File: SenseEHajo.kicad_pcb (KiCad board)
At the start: 2 copper layers, 141 x 56.9 mm, 104 parts, among them IC1 AP3012, IC2 MCP3221, IC3 74LVC1G125, IC4 K814P, IC5 74LVC1G125, IC6 74LVC1G125, IC7 74LVC1G10, J1 Conn_01x02_Male, J2 REED, J3 RTC ( DS3231), J4 Heizung L, J5 Pumpe L, J6 Conn_01x05, J7 L, J8 N, J9 Prog, Q1 BSS138, SW2 SW1 ( Boot ), SW3 MACHINE_SW2, SW4 MACHINE_SW3, T1 QJ8025, T2 QJ8025, U1 ESP32-WROOM-32, U2 MCP6001-OT, U3 MOC3043M, U4 MOC3043M, U5 MCP6001-OT, U6 LM1117-3.3

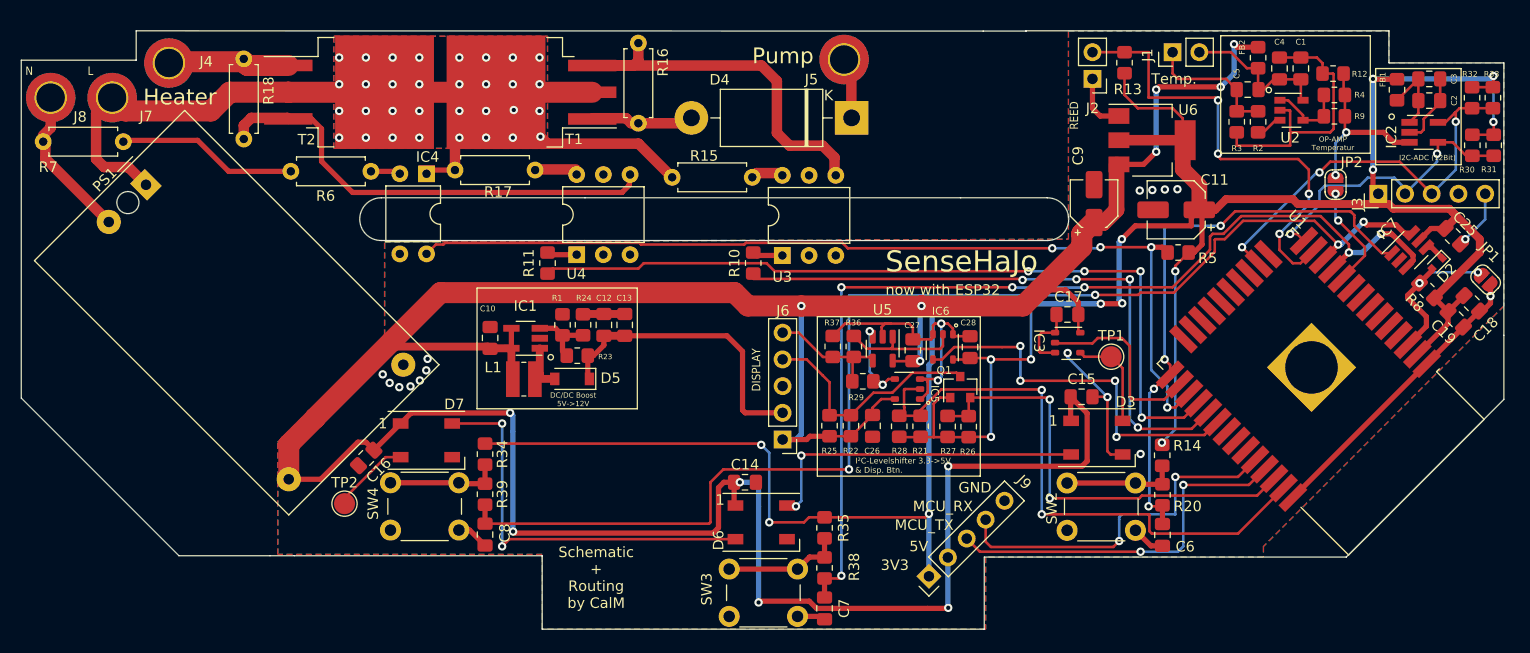
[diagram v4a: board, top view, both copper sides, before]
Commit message: Fix Display BTP senese for press
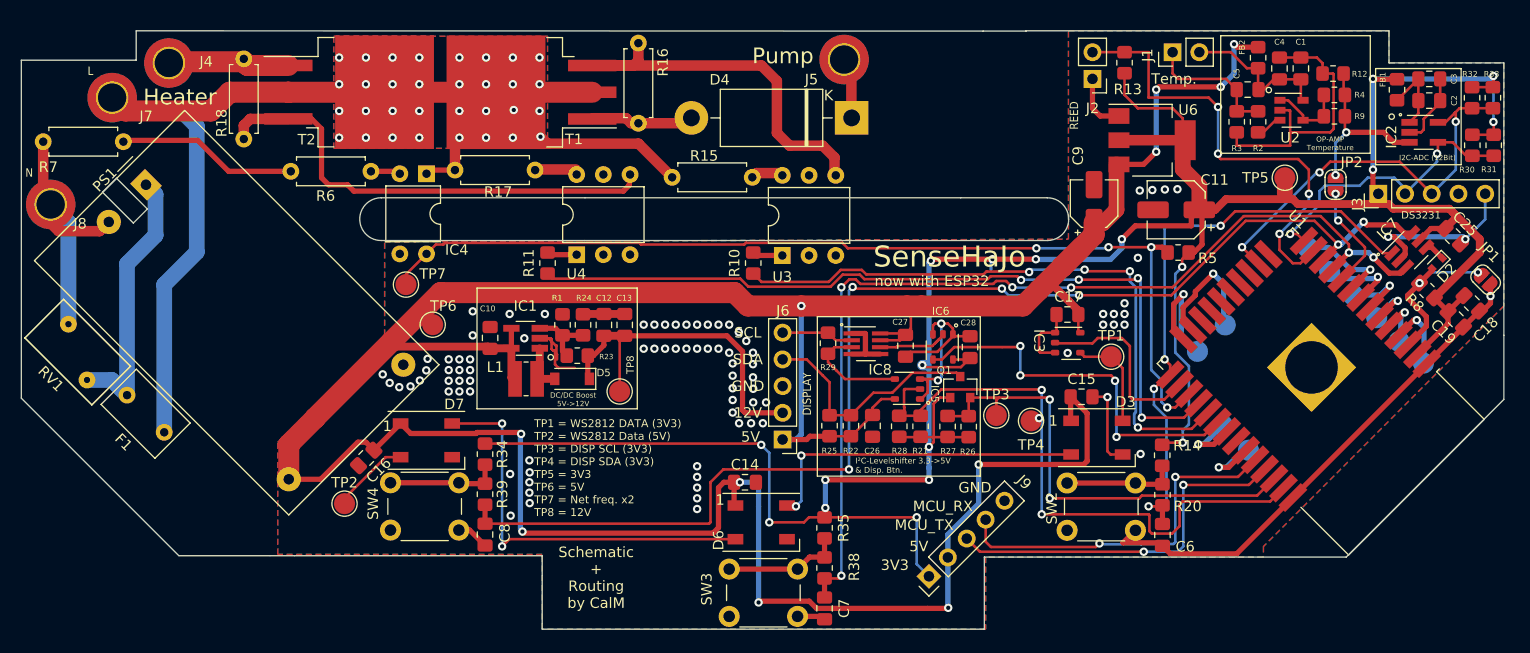
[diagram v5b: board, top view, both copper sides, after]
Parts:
- removed R36: 10k, Resistor_SMD:R_0805_2012Metric_Pad1.20x1.40mm_HandSolder
- removed R37: 1k, Resistor_SMD:R_0805_2012Metric_Pad1.20x1.40mm_HandSolder
- removed REF**: MountingHole_2.1mm, MountingHole:MountingHole_2.1mm
- removed U5: MCP6001-OT, Package_TO_SOT_SMD:SOT-23-5
- added F1: 0.5A / 230VAC, Capacitor_THT:C_Rect_L7.0mm_W4.5mm_P5.00mm, F.Cu at (36.7, 58.5)
- added IC8: INA350ABS, Package_TO_SOT_SMD:SOT-23-8_Handsoldering, F.Cu at (103.4, 50.1)
- added IO15: IO32, TestPoint:TestPoint_Pad_D2.0mm, B.Cu at (137.6, 48.3)
- added IO19: IO32, TestPoint:TestPoint_Pad_D2.0mm, B.Cu at (137.3, 57.8)
- added IO2: IO32, TestPoint:TestPoint_Pad_D2.0mm, B.Cu at (135.0, 50.8)
- added IO21: IO32, TestPoint:TestPoint_Pad_D2.0mm, B.Cu at (139.8, 60.2)
- added IO32: IO32, TestPoint:TestPoint_Pad_D2.0mm, B.Cu at (147.5, 43.2)
- added IO33: IO32, TestPoint:TestPoint_Pad_D2.0mm, B.Cu at (145.4, 40.9)
- added IO34: IO32, TestPoint:TestPoint_Pad_D2.0mm, B.Cu at (152.0, 47.6)
- added IO35: IO32, TestPoint:TestPoint_Pad_D2.0mm, B.Cu at (149.7, 45.4)
- added RV1: Varistor 10D561, Varistor:RV_Disc_D9mm_W5.2mm_P5mm, F.Cu at (27.6, 48.2)
- added S_VN1: IO32, TestPoint:TestPoint_Pad_D2.0mm, B.Cu at (154.1, 49.9)
- added S_VP1: IO32, TestPoint:TestPoint_Pad_D2.0mm, B.Cu at (156.4, 51.9)
- added TP3: I2C_DISP_SDA_3V3, TestPoint:TestPoint_Pad_D2.0mm, F.Cu at (115.8, 56.9)
- added TP4: I2C_DISP_SCL_3V3, TestPoint:TestPoint_Pad_D2.0mm, F.Cu at (119.1, 57.4)
- added TP5: 3V3, TestPoint:TestPoint_Pad_D2.0mm, F.Cu at (143.3, 34.3)
- added TP6: 5V, TestPoint:TestPoint_Pad_D2.0mm, F.Cu at (62.2, 48.3)
- added TP7: MAINS Halvewaves, TestPoint:TestPoint_Pad_D2.0mm, F.Cu at (59.7, 44.5)
- added TP8: 12V, TestPoint:TestPoint_Pad_D2.0mm, F.Cu at (80.0, 54.6)
- moved J8 10.2 mm to (25.9, 36.8)
- moved R29 4.91 mm to (99.8, 50.0), turned to -90 degrees
- moved C27 0.82 mm to (107.2, 50.3), turned to -90 degrees
- moved L1 0.21 mm to (71.1, 53.4)
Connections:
- PS1 pad 1: L_230V -> Net-(PS1-AC/L)
- U1 pad 23: unconnected-(U1-Pad23) -> Net-(U1-IO15)
- U1 pad 24: unconnected-(U1-Pad24) -> Net-(U1-IO2)
- U1 pad 31: unconnected-(U1-Pad31) -> Net-(U1-IO19)
- U1 pad 33: unconnected-(U1-Pad33) -> Net-(U1-IO21)
- U1 pad 4: unconnected-(U1-Pad4) -> Net-(U1-SENSOR_VP)
- U1 pad 5: unconnected-(U1-Pad5) -> Net-(U1-SENSOR_VN)
- U1 pad 6: unconnected-(U1-Pad6) -> Net-(U1-IO34)
- U1 pad 7: unconnected-(U1-Pad7) -> Net-(U1-IO35)
- U1 pad 8: unconnected-(U1-Pad8) -> Net-(U1-IO32)
- U1 pad 9: unconnected-(U1-Pad9) -> Net-(U1-IO33)
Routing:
- net GND: track 135.1 -> 164.7 mm, vias 18 -> 90
- net L_230V: track 83.0 -> 110.3 mm
- net Net-(PS1-AC/L): track 0.00 -> 25.9 mm
- net Net-(U1-IO15): track 0.00 -> 12.4 mm, vias 0 -> 1
- net N_230V: track 14.2 -> 26.3 mm
- net Net-(U1-IO2): track 0.00 -> 11.3 mm, vias 0 -> 1
- net Net-(U1-IO33): track 0.00 -> 9.36 mm, vias 0 -> 1
- net Net-(U1-IO32): track 0.00 -> 7.57 mm, vias 0 -> 1
- net +12V: track 28.4 -> 35.2 mm
- net Net-(U1-SENSOR_VP): track 0.00 -> 6.71 mm, vias 0 -> 1
- net Net-(U1-IO35): track 0.00 -> 6.68 mm, vias 0 -> 1
- net Net-(U1-IO21): track 0.00 -> 6.41 mm, vias 0 -> 1
- net Net-(U1-IO19): track 0.00 -> 6.28 mm, vias 0 -> 1
- net +3V3: track 283.5 -> 277.7 mm, vias 15 -> 18
- net SCL_DSP: track 12.4 -> 6.72 mm
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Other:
- outline, holes or cut-outs redrawn
- board text added: "12V"
- board text added: "DS3231"
- board text added: "OP-AMP Temperature"
- board text added: "SCL"
- board text added: "SDA"
- board text added: "SLC"
- board text added: "TP1 = WS2812 DATA (3V3) TP2 = WS2812 Data (5V) TP3 = DISP SCL (3V3) TP4 = DISP SDA (3V3) TP5 = 3V3 TP6 = 5V TP7 = Net freq. x2 TP8 = 12V"
- board text removed: "OP-AMP Temperatur"
